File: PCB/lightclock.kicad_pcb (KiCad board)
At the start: 2 copper layers, 133 x 133 mm, 198 parts, among them M1 Fan, Q1 NPN, Q2 AO3401A, Q3 AO3400A, SW1 TP15822637, U1 STP24DP05BTR, U11 TPS54232DR, U12 MPR121QR2, U13 PM254-1-06-W-8.5, U2 CH224K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

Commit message: added spare GPIO pads & ventilation for enclosure back
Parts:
- added 24: ExtraGPIO, TestPoint:TestPoint_THTPad_1.5x1.5mm_Drill0.7mm, B.Cu at (117.6, 79.9)
- added 25: ExtraGPIO, TestPoint:TestPoint_THTPad_1.5x1.5mm_Drill0.7mm, B.Cu at (117.6, 77.2)
- added 26: ExtraGPIO, TestPoint:TestPoint_THTPad_1.5x1.5mm_Drill0.7mm, B.Cu at (120.2, 79.9)
- added 27: ExtraGPIO, TestPoint:TestPoint_THTPad_1.5x1.5mm_Drill0.7mm, B.Cu at (120.2, 77.2)
- moved R34 1.27 mm to (121.2, 112.8)
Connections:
- U4 pad 36: unconnected-(U4-GPIO24-Pad36) -> Net-(U4-GPIO24)
- U4 pad 37: unconnected-(U4-GPIO25-Pad37) -> Net-(U4-GPIO25)
- U4 pad 38: unconnected-(U4-GPIO26/ADC0-Pad38) -> Net-(U4-GPIO26/ADC0)
- U4 pad 39: unconnected-(U4-GPIO27/ADC1-Pad39) -> Net-(U4-GPIO27/ADC1)
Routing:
- net Net-(U4-GPIO25): track 0.00 -> 38.7 mm
- net Net-(U4-GPIO27/ADC1): track 0.00 -> 37.2 mm
- net Net-(U4-GPIO24): track 0.00 -> 36.5 mm
- net Net-(U4-GPIO26/ADC0): track 0.00 -> 34.5 mm
- net /GPIO19: track 82.0 -> 83.8 mm
- net /GPIO22: track 4.21 -> 3.25 mm
- net Net-(BUZZER1-+): track 46.3 -> 46.8 mm
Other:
- board text added: "GPIO"

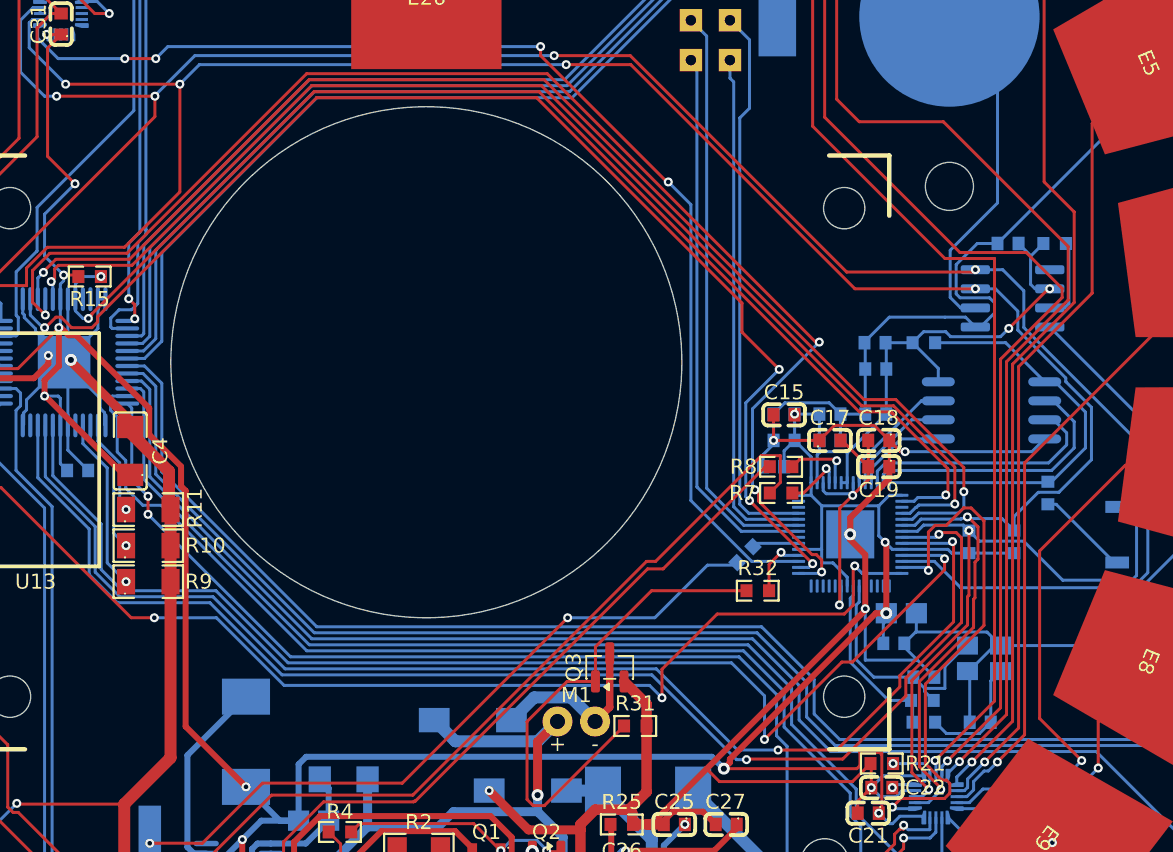
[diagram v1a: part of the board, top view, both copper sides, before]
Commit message: connected INT pin on RTC to RP2040 for alarms
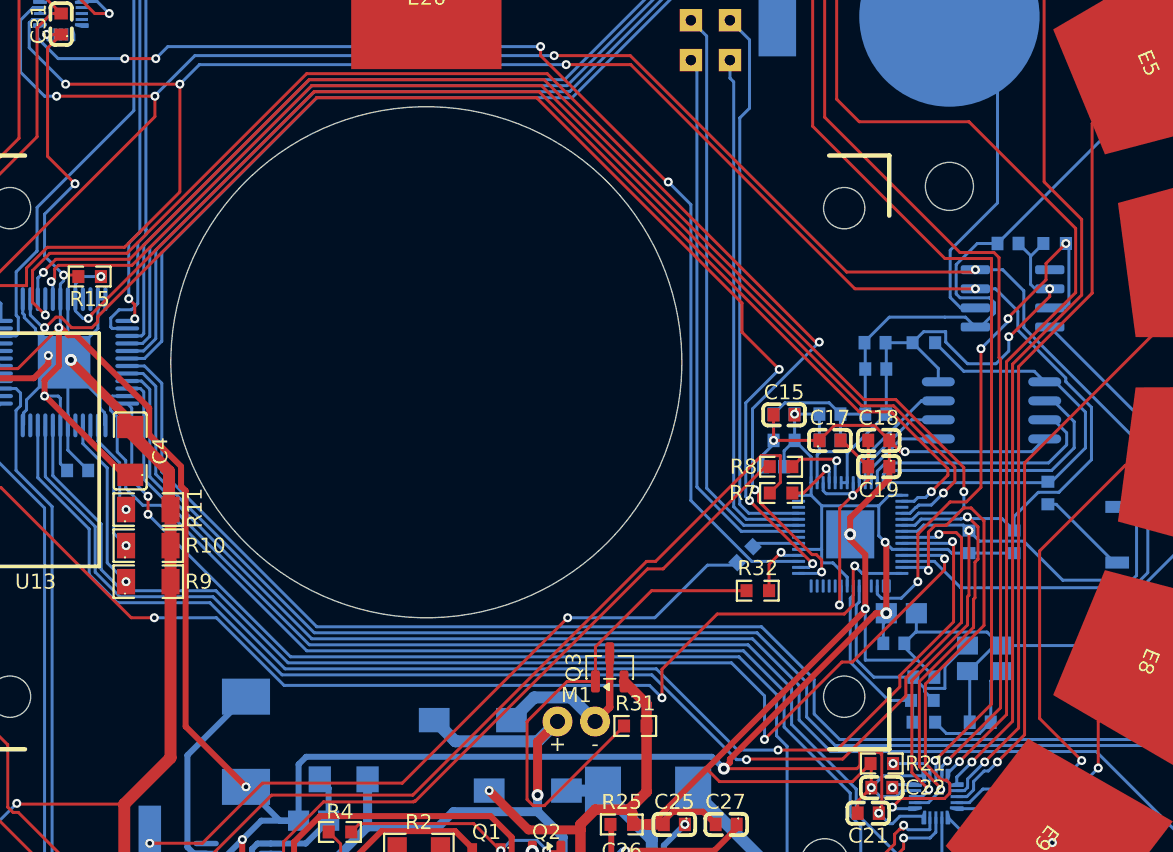
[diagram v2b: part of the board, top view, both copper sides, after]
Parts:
- renumbered 24 to GP24, 25 to GP25, 26 to GP26, 27 to GP27
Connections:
- R18 pad 2: Net-(U7-~{INT}/SQW) -> /GPIO14
- U4 pad 17: unconnected-(U4-GPIO14-Pad17) -> /GPIO14
- U7 pad 3: Net-(U7-~{INT}/SQW) -> /GPIO14
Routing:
- net /GPIO14: track 0.00 -> 36.5 mm, vias 0 -> 4
- net Net-(U7-~{INT}/SQW): track 5.47 -> 0.00 mm
- net Net-(U8-ELE1): track 91.1 -> 86.5 mm
- net +3V3: track 268.9 -> 271.7 mm
- net Net-(U8-ELE2): track 84.1 -> 85.5 mm
- net /GPIO2: track 83.8 -> 83.0 mm
- net /GPIO0: track 83.5 -> 82.8 mm
